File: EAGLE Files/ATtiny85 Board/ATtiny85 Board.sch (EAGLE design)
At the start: 10 parts

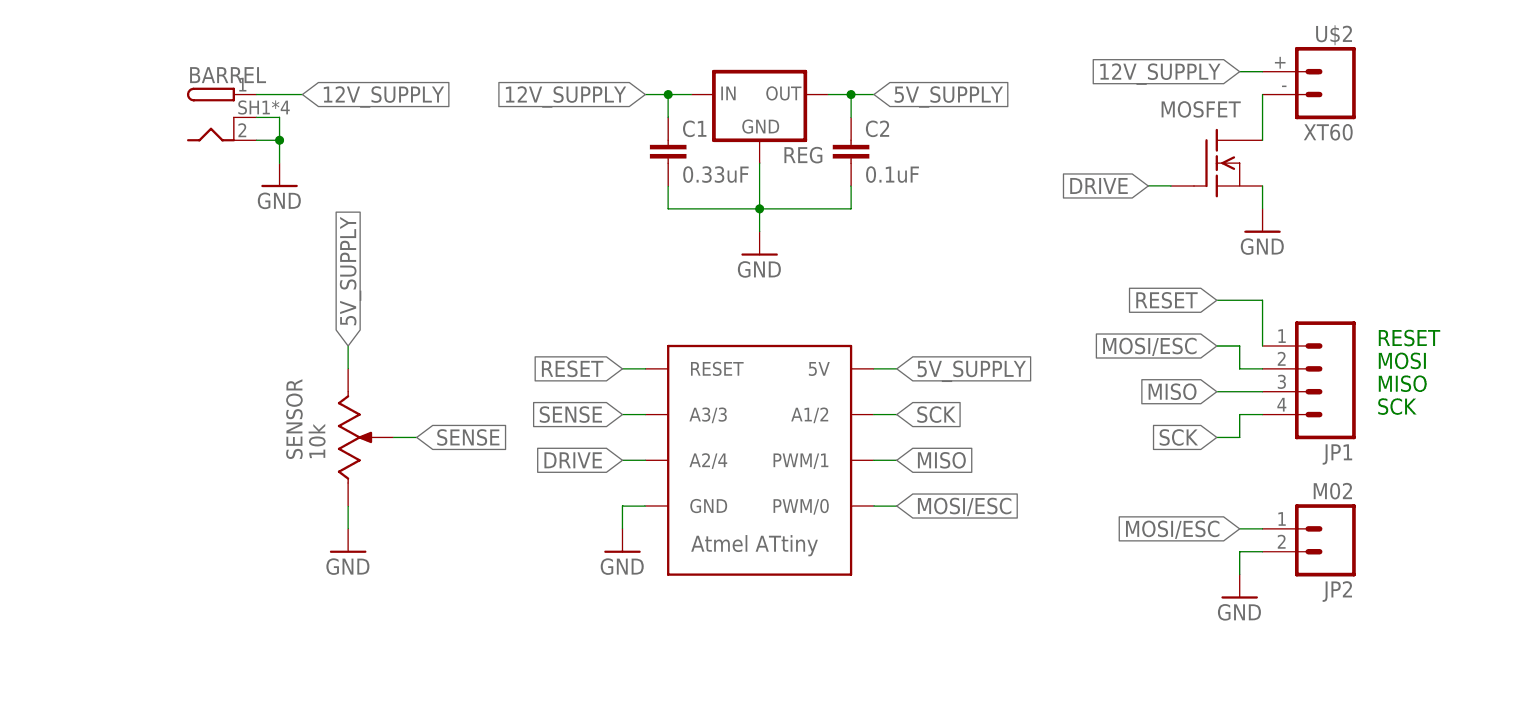
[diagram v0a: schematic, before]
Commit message: Enlarged and repositioned vias for easier milling and soldering
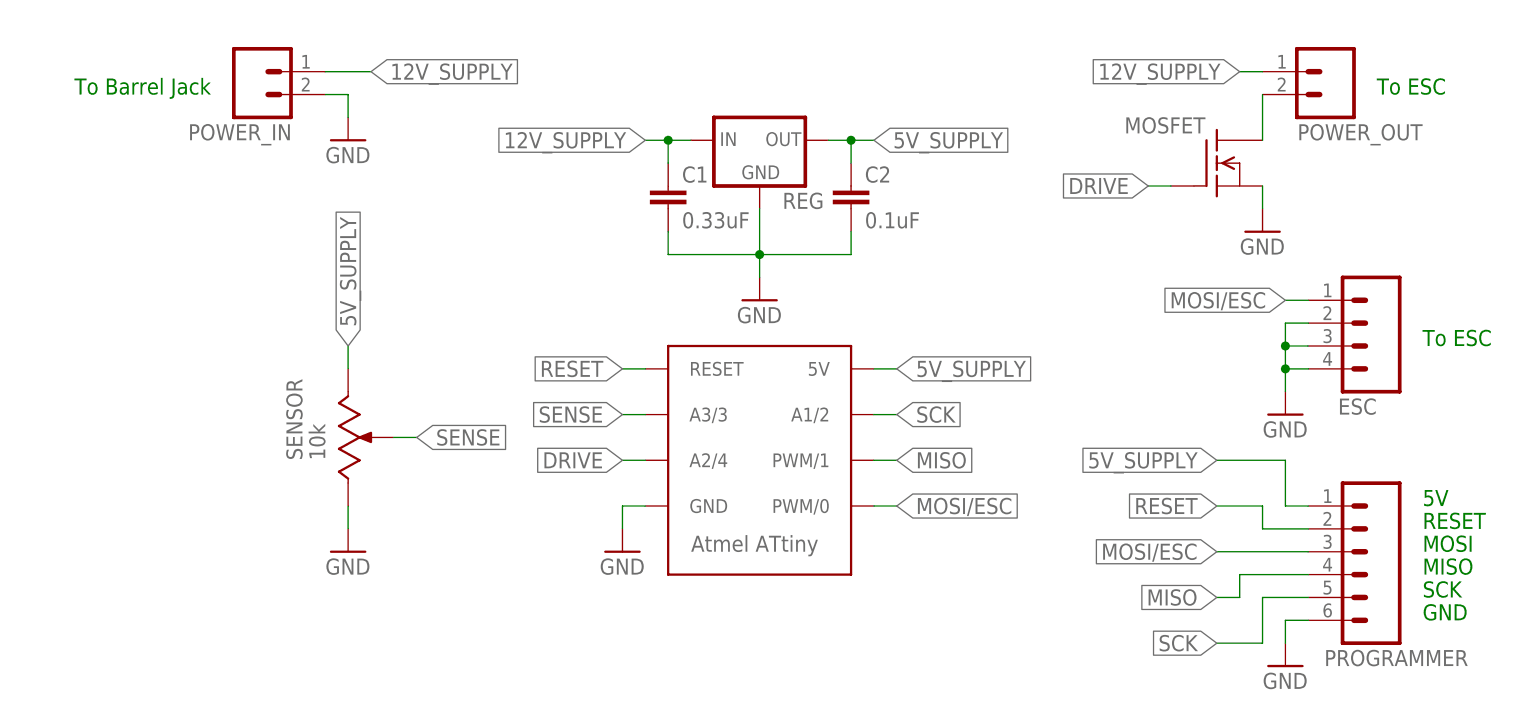
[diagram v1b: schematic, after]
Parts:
- removed BARREL: PJ-082BH, Controls Library:PJ-082BH
- removed JP1: (no value), Controls Library:M04
- removed JP2: M02, Controls Library:M02
- removed U$2: XT60, Controls Library:XT60
- added ESC: (no value), Controls Library:M04
- added POWER_IN, POWER_OUT: M02, Controls Library:M02
- added PROGRAMMER: (no value), Controls Library:M06
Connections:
- net 12V_SUPPLY: now also POWER_IN.1, POWER_OUT.1; no longer BARREL.PWR, U$2.2
- net 5V_SUPPLY: now also PROGRAMMER.1
- net GND: now also ESC.2, ESC.3, ESC.4, POWER_IN.2, PROGRAMMER.6; no longer BARREL.GND, BARREL.SHIELD, JP2.2
- net MISO: now also PROGRAMMER.4; no longer JP1.3
- net MOSI/ESC: now also ESC.1, PROGRAMMER.3; no longer JP1.2, JP2.1
- net N$3: now also POWER_OUT.2; no longer U$2.1
- net RESET: now also PROGRAMMER.2; no longer JP1.1
- net SCK: now also PROGRAMMER.5; no longer JP1.4
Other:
- note added: "5V"
- note added: "GND"
- note added: "To Barrel Jack"
- note added: "To ESC"
- moved on the sheet: C1, C2, REG
